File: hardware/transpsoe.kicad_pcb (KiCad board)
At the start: 2 copper layers, 102.2 x 51.5 mm, 107 parts, among them J1 Input CV 1, J10 AudioJack2_SwitchT, J11 AudioJack2_SwitchT, J12 Conn_01x08_Female, J13 Conn_01x08_Female, J14 Conn_01x08_Male, J15 Conn_01x08_Male, J2 Input CV 2, J3 AudioJack2_SwitchT, J4 AudioJack2_SwitchT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

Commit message: Rotate rotary knob so pin 1 is facing up
This brings it into alignment with the panel's 0 indicator
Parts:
- moved R73 18.1 mm to (102.5, 109.5), turned to 180 degrees
- moved R76 18.1 mm to (108.0, 119.8), turned to 0 degrees
- moved R78 18.1 mm to (116.0, 119.8), turned to 0 degrees
- moved R75 18.0 mm to (102.5, 113.0), turned to 180 degrees
- moved R79 17.4 mm to (120.2, 113.2), turned to 90 degrees
- moved R72 17.3 mm to (108.0, 102.8), turned to 180 degrees
- moved R74 17.3 mm to (102.5, 111.2), turned to 180 degrees
- moved R80 17.1 mm to (120.2, 109.2), turned to 90 degrees
- moved R82 16.4 mm to (112.0, 102.8), turned to 180 degrees
- moved R81 16.4 mm to (116.0, 102.8), turned to 180 degrees
- moved R77 16.2 mm to (112.0, 119.8), turned to 0 degrees
- turned SW1 to 195 degrees
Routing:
- net Net-(R75-Pad2): track 9.46 -> 14.6 mm
- net Net-(R80-Pad2): track 6.41 -> 10.9 mm
- net Net-(R72-Pad2): track 7.89 -> 11.3 mm
- net SW1.b: track 68.1 -> 64.7 mm
- net Net-(R76-Pad2): track 4.93 -> 7.19 mm
- net Net-(R81-Pad2): track 9.37 -> 7.15 mm
- net Net-(R74-Pad2): track 5.14 -> 7.18 mm
- net Net-(R78-Pad2): track 12.5 -> 10.6 mm
- net Net-(R77-Pad2): track 4.93 -> 6.84 mm
- net SW1.a: track 41.7 -> 39.9 mm
- net Net-(R72-Pad1): track 3.21 -> 4.59 mm
- net Net-(R73-Pad2): track 7.50 -> 6.25 mm

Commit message: Use different nets for main versus jack board
This gets rid of the 14 spurious "Unconnected Items" DRCs, and makes
it more explicit which parts are on which board.
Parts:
- J1: value Input CV 1 -> AudioJack2_SwitchT
- J2: value Input CV 2 -> AudioJack2_SwitchT
- turned R24 to 90 degrees
- turned SW1 to 0 degrees
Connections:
- J1 pad S: GND -> Jacks-GND
- J1 pad T: /J1.T -> Jacks-J1.T
- J10 pad S: GND -> Jacks-GND
- J10 pad T: /J10.T -> Jacks-J10.T
- J11 pad S: GND -> Jacks-GND
- J11 pad T: /J11.T -> Jacks-J11.T
- J12 pad 1: SW1.a -> Jacks-SW1.a
- J12 pad 2: SW1.b -> Jacks-SW1.b
- J12 pad 3: GND -> Jacks-GND
- J12 pad 4: /J1.T -> Jacks-J1.T
- J12 pad 5: /SUM_SW.out -> Jacks-SUM_SW.out
- J12 pad 6: /J2.T -> Jacks-J2.T
- J12 pad 7: /A+S -> Jacks-A+S
- J12 pad 8: /J5.T -> Jacks-J5.T
- J13 pad 1: /J4.T -> Jacks-J4.T
- J13 pad 2: /J8.T -> Jacks-J8.T
- J13 pad 3: /J9.T -> Jacks-J9.T
- J13 pad 4: GND -> Jacks-GND
- J13 pad 5: GND -> Jacks-GND
- J13 pad 6: /J11.T -> Jacks-J11.T
- J13 pad 7: /J10.T -> Jacks-J10.T
- J13 pad 8: /J6.T -> Jacks-J6.T
- J2 pad S: GND -> Jacks-GND
- J2 pad T: /J2.T -> Jacks-J2.T
- J3 pad S: GND -> Jacks-GND
- J3 pad T: /J3.T -> Net-(J3-PadT)
- J4 pad S: GND -> Jacks-GND
- J4 pad T: /J4.T -> Jacks-J4.T
- J5 pad S: GND -> Jacks-GND
- J5 pad T: /J5.T -> Jacks-J5.T
- J6 pad S: GND -> Jacks-GND
- J6 pad T: /J6.T -> Jacks-J6.T
- J8 pad S: GND -> Jacks-GND
- J8 pad T: /J8.T -> Jacks-J8.T
- J9 pad S: GND -> Jacks-GND
- J9 pad T: /J9.T -> Jacks-J9.T
- R16 pad 2: /A+S -> Jacks-A+S
- R24 pad 1: /A+S -> Net-(J3-PadT)
- R24 pad 2: /J3.T -> Jacks-A+S
- R3 pad 1: GND -> Jacks-GND
- R82 pad 2: SW1.b -> Jacks-SW1.b
- SW1 pad 1: SW1.b -> Jacks-SW1.b
- SW1 pad 13: SW1.a -> Jacks-SW1.a
- SW2 pad 2: /SUM_SW.out -> Jacks-SUM_SW.out
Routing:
- net /J4.T: track 67.4 -> 26.2 mm
- net Jacks-J4.T: track 0.00 -> 41.2 mm
- net Jacks-J6.T: track 0.00 -> 37.9 mm
- net /J6.T: track 59.4 -> 21.6 mm
- net Jacks-J5.T: track 0.00 -> 37.1 mm
- net /J5.T: track 83.3 -> 46.2 mm
- net Jacks-J10.T: track 0.00 -> 26.3 mm
- net /J10.T: track 31.1 -> 4.79 mm
- net /J8.T: track 29.7 -> 7.25 mm
- net Jacks-J8.T: track 0.00 -> 22.4 mm
- net /A+S: track 70.1 -> 47.9 mm
- net Jacks-A+S: track 0.00 -> 22.2 mm
- net Jacks-GND: track 0.00 -> 19.8 mm, vias 0 -> 3
- net GND: track 89.4 -> 69.6 mm, vias 35 -> 32
- net SW1.a: track 39.9 -> 21.1 mm
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- added copper zone on F.Cu, net Jacks-GND

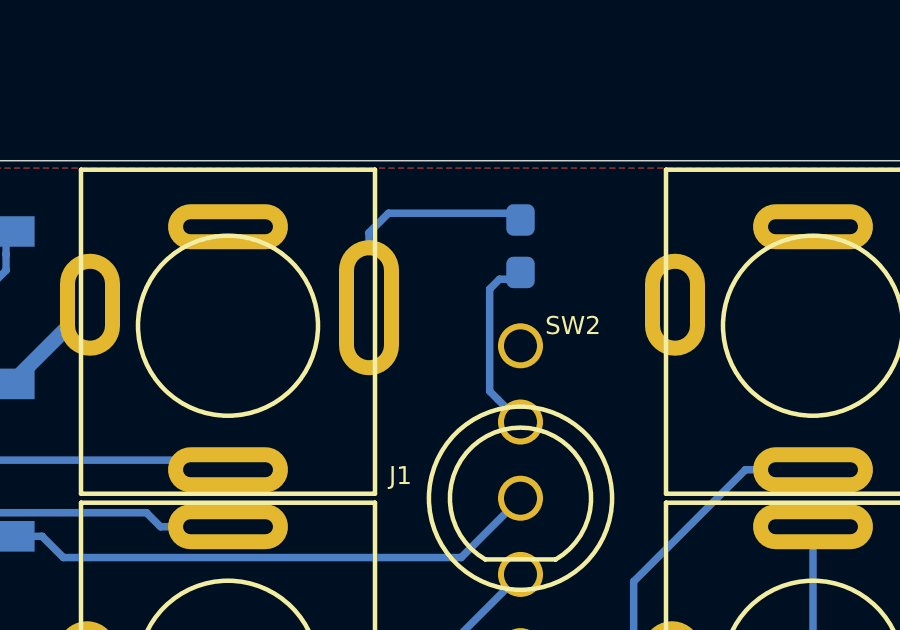
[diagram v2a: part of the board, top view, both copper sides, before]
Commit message: Remove unnecessary circuit on "up" position of toggle switch
An open circuit will work just as well as a resistor to ground, with
fewer parts.
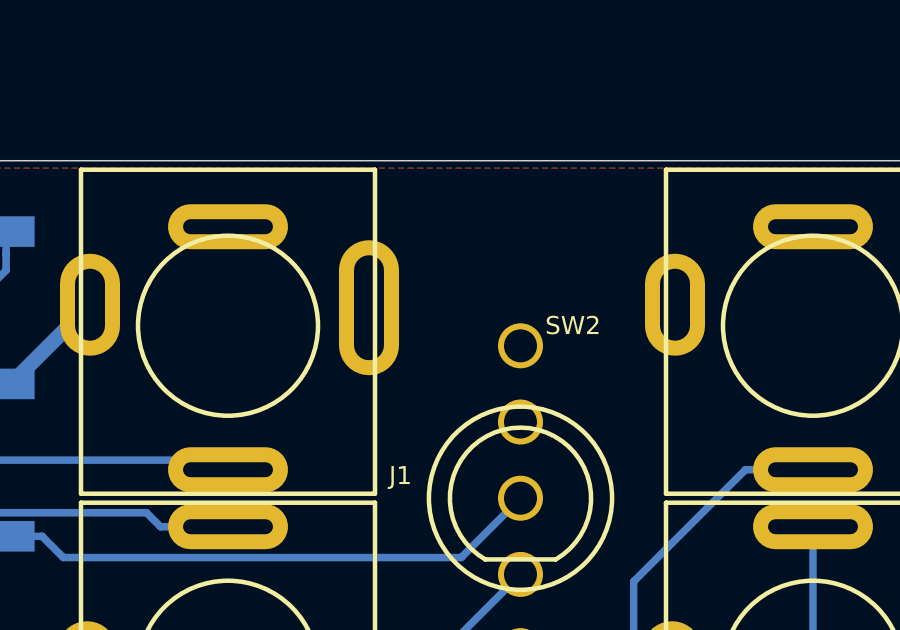
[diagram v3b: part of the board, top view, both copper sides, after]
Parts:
- removed R3: 100k, Resistor_SMD:R_0603_1608Metric_Pad1.05x0.95mm_HandSolder
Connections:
- SW2 pad 1: Net-(R3-Pad2) -> (no net)
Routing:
- net Jacks-GND: track 19.8 -> 12.0 mm
- net Net-(R3-Pad2): track 6.02 -> 0.00 mm

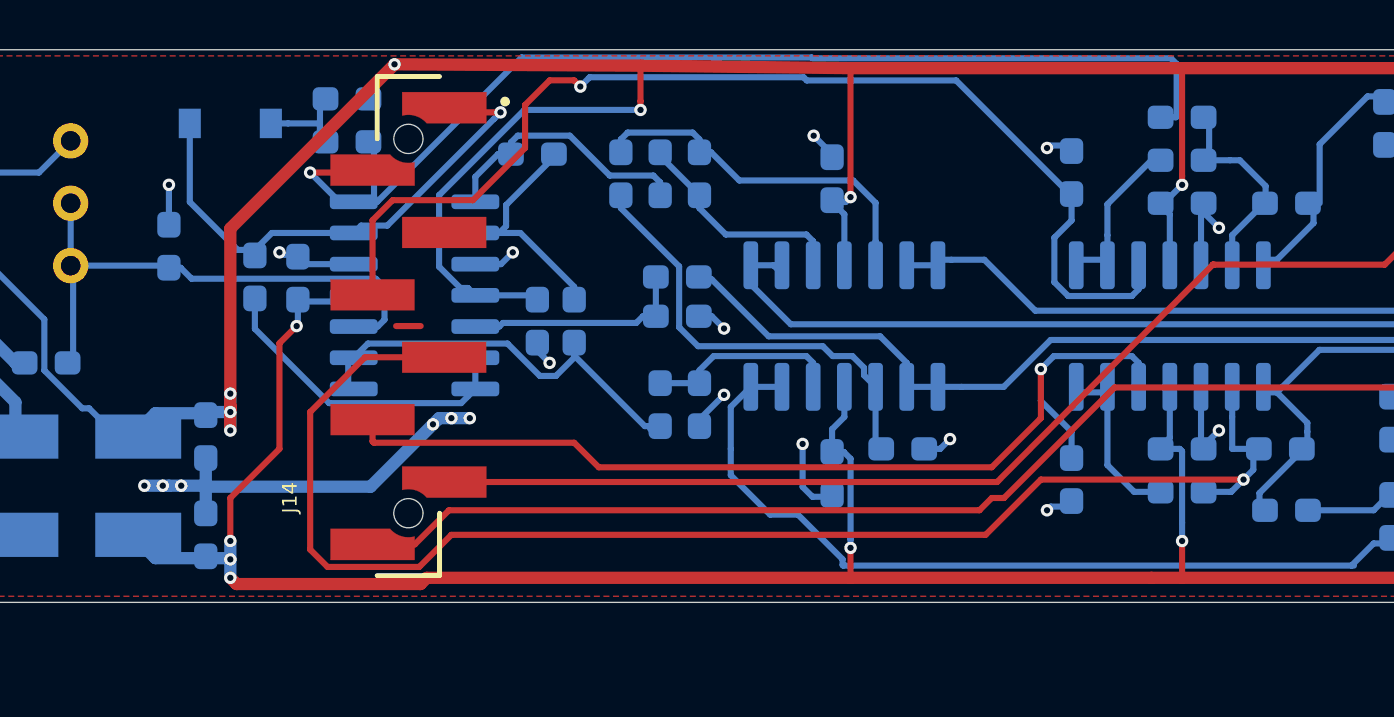
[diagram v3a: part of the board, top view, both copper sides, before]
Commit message: Rework semitone circuit
- Flip the polarity of the voltage limiter, which accidentally wasn't
  inverted when the subcircuit's output polarity was inverted earlier
  in the design work.
- Add a trimpot to the semitone voltage reference, to compensate for
  various sources of error
- Add to the spice model to allow testing the error on the semitone
  output
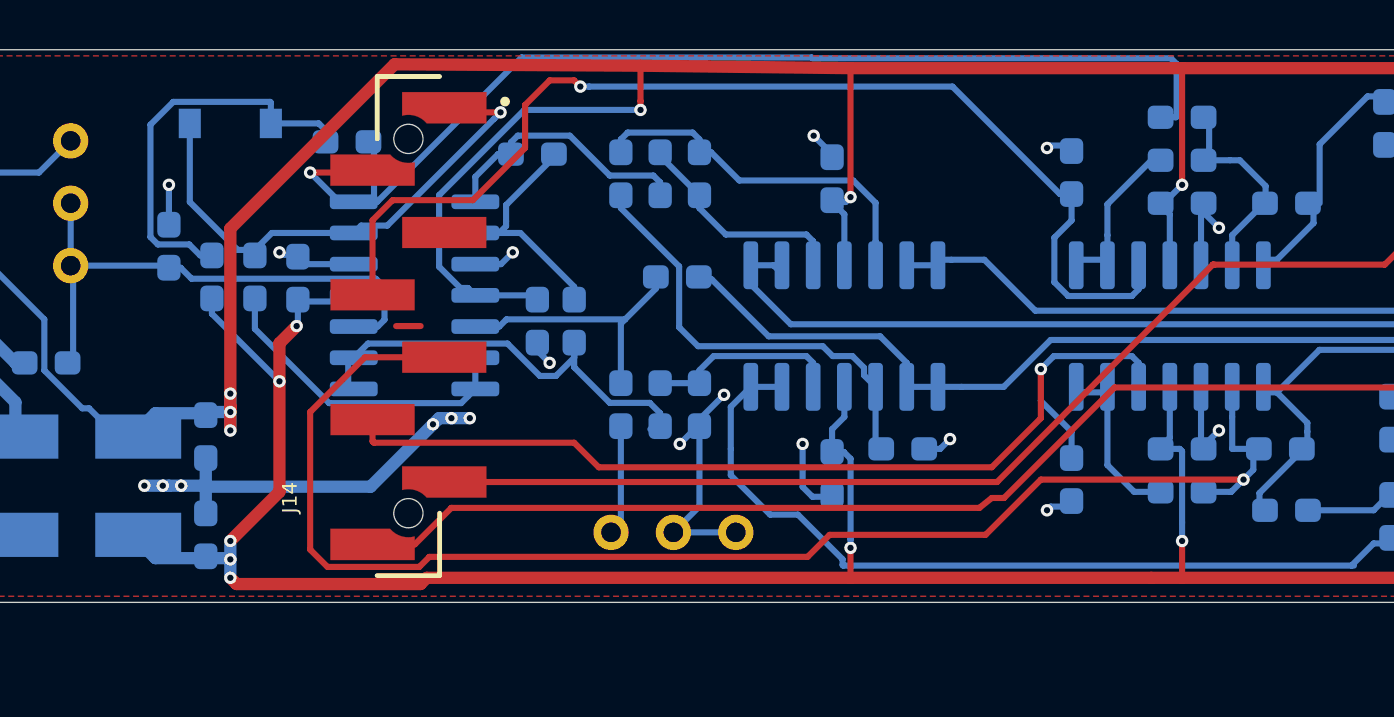
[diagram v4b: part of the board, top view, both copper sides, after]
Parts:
- added RV2: 2k, Potentiometer_THT:Potentiometer_Bourns_3296W_Vertical, B.Cu at (133.0, 90.7)
- R68: value 10k -> 9.1k
- moved R71 9.10 mm to (116.8, 80.2), turned to 270 degrees
- moved R68 4.27 mm to (133.4, 85.5), turned to 90 degrees
- turned D3 to 0 degrees
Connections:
- D3 pad 1: Net-(D3-Pad1) -> SW1.a
- D3 pad 2: SW1.a -> Net-(D3-Pad2)
- J1 pad TN: (no net) -> Net-(J1-PadTN)
- J10 pad TN: (no net) -> Net-(J10-PadTN)
- J11 pad TN: (no net) -> Net-(J11-PadTN)
- J2 pad TN: (no net) -> Net-(J2-PadTN)
- J3 pad TN: (no net) -> Net-(J3-PadTN)
- J4 pad TN: (no net) -> Net-(J4-PadTN)
- J5 pad TN: (no net) -> Net-(J5-PadTN)
- J6 pad TN: (no net) -> Net-(J6-PadTN)
- J8 pad TN: (no net) -> Net-(J8-PadTN)
- J9 pad TN: (no net) -> Net-(J9-PadTN)
- R68 pad 1: GND -> Net-(R68-Pad1)
- R70 pad 2: Net-(D3-Pad1) -> Net-(D3-Pad2)
- R71 pad 1: Net-(D3-Pad1) -> Net-(D3-Pad2)
- R71 pad 2: +12V -> -12V
- SW2 pad 1: (no net) -> Net-(SW2-Pad1)
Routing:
- net Net-(D3-Pad2): track 0.00 -> 16.3 mm
- net GND: track 69.6 -> 76.7 mm
- net -12V: track 124.1 -> 128.7 mm, vias 8 -> 9
- net Net-(R68-Pad1): track 0.00 -> 4.49 mm
- net Net-(D3-Pad1): track 4.47 -> 0.00 mm
- net Net-(R67-Pad1): track 8.82 -> 11.1 mm
- net +12V: track 164.4 -> 162.7 mm, vias 9 -> 8
- net Net-(R51-Pad2): track 18.1 -> 18.7 mm

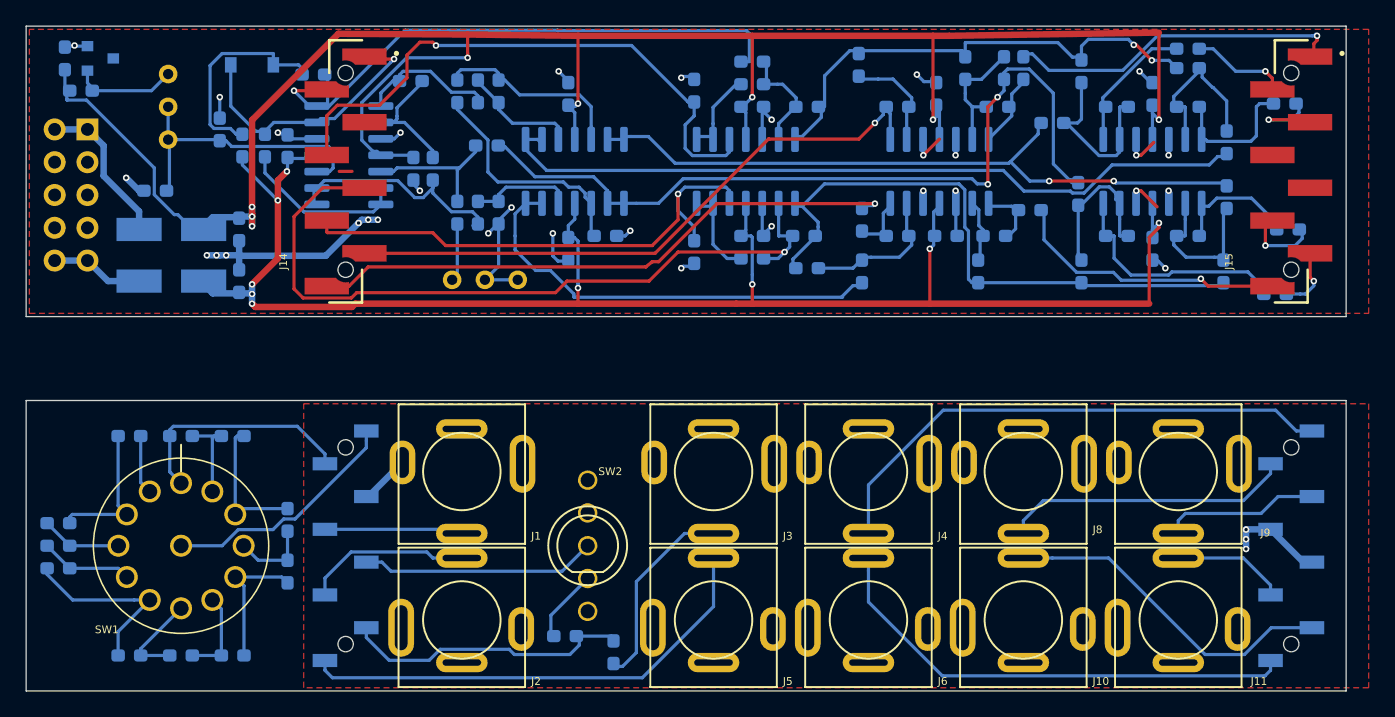
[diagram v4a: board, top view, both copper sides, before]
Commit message: Narrow boards by 0.5mm
It's not a lot, but it gives us a little extra margin in fit-up
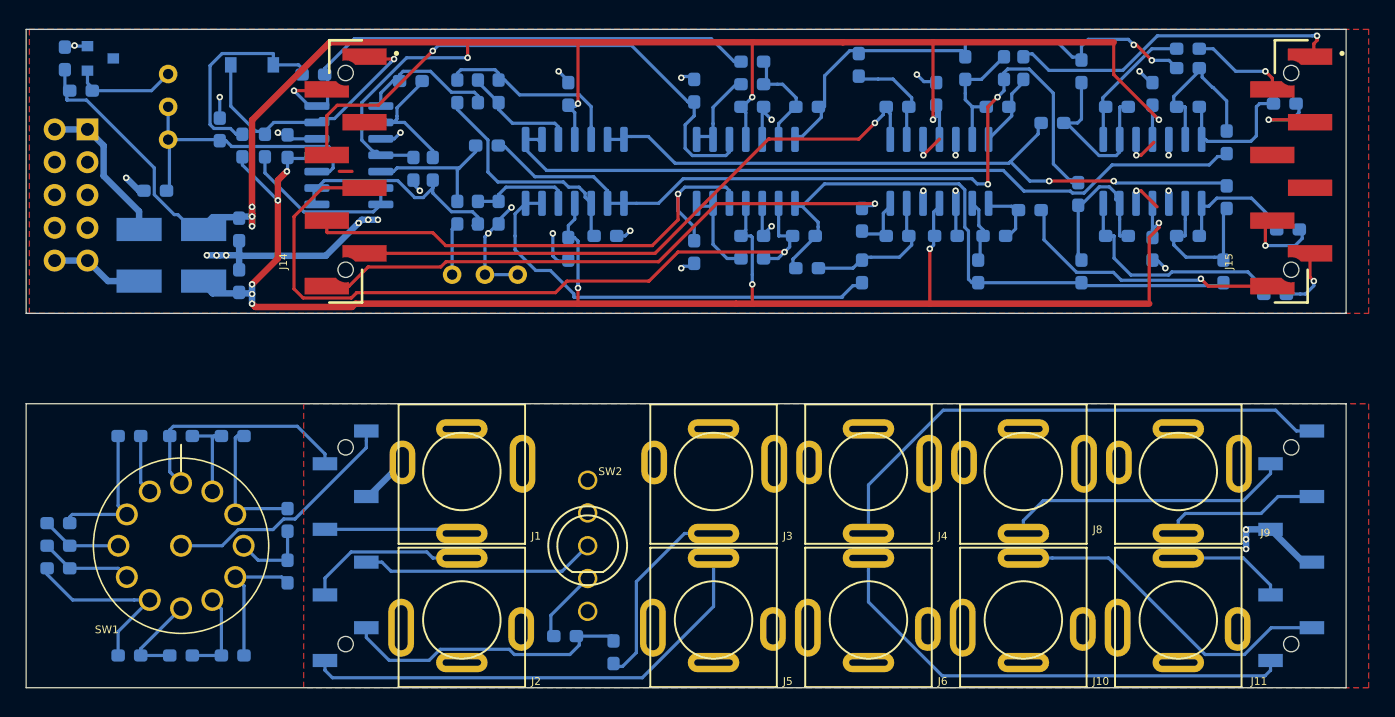
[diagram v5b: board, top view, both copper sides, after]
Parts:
- moved RV2 0.40 mm to (133.0, 90.2)
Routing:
- net +12V: track 162.7 -> 157.5 mm
- net SW1.b: track 46.4 -> 42.5 mm
- net GND: track 76.7 -> 75.3 mm
- net /J1.T: track 46.4 -> 45.2 mm
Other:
- board size 102.2 x 51.5 mm -> 102.2 x 51 mm
